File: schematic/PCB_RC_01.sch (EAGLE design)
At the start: 0 parts

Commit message: Completed PCB
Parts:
- added 12V, 5V, JET: GRN, led:LED5MM
- added 3V3: YEL, led:LED5MM
- added F1: 10A, fuse:FUSEBLANK_5X20MM
- added F2: 5A, fuse:FUSEBLANK_5X20MM
- added IC1: 3V3REG, pinhead:PINHD-1X4
- added IC2: 5VREG, SparkFun-IC-Power:V_REG_LD1117VXX
- added IC3-1, IC3-2: 12VREG, pinhead:PINHD-1X4
- added J1: 282836-2, 5mm Terminal Block:282836-2
- added J2: JETSON, 5mm Terminal Block:282836-2
- added J3: ARDUINO, 5mm Terminal Block:282836-2
- added J4: RESV, 5mm Terminal Block:282836-2
- added J6: USB1, SparkFun-Connectors:USB_B_PTH
- added J7: USB2, SparkFun-Connectors:USB_B_PTH
- added JP1: 5V PORT, pinhead:PINHD-2X5
- added JP2: 3V3 PORT, pinhead:PINHD-2X5
- added MOT, PWR: RED, led:LED5MM
- added R1, R2, R3, R4, R5, R6: 10K, rcl:R-US_V234/12
- added SW1: PWR, switch:2P2T
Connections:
- new net 12VREG: F2.1, IC3-1.3, IC3-1.4, J3.1, J4.1, R4.1
- new net 3V3REG: IC1.2, JP2.1, JP2.3, JP2.5, JP2.7, JP2.9, R3.1
- new net 5VREG: IC2.OUT, J6.VBUS, J7.VBUS, JP1.1, JP1.3, JP1.5, JP1.7, JP1.9, R2.1
- new net GND: 12V.C, 3V3.C, 5V.C, IC1.1, IC2.GND, IC3-1.1, IC3-1.2, IC3-2.1, IC3-2.2, J1.2, J2.2, J3.2, J4.2, J6.GND, J7.GND, JET.C, JP1.10, JP1.2, JP1.4, JP1.6, JP1.8, JP2.10, JP2.2, JP2.4, JP2.6, JP2.8, MOT.C, PWR.C, SW1.2.1, SW1.2.2
- new net JETSON: F2.2, J2.1, R5.1
- new net N$1: PWR.A, R1.2
- new net N$2: 5V.A, R2.2
- new net N$3: 3V3.A, R3.2
- new net N$4: 12V.A, R4.2
- new net N$5: MOT.A, R5.2
- new net N$6: JET.A, R6.2
- new net VBATT: J1.1, SW1.1.1, SW1.1.2
- new net VFUSE: F1.2, IC1.3, IC1.4, IC2.IN, IC3-2.3, IC3-2.4, R6.1
- new net VSWITCH: F1.1, R1.1, SW1.3.1, SW1.3.2

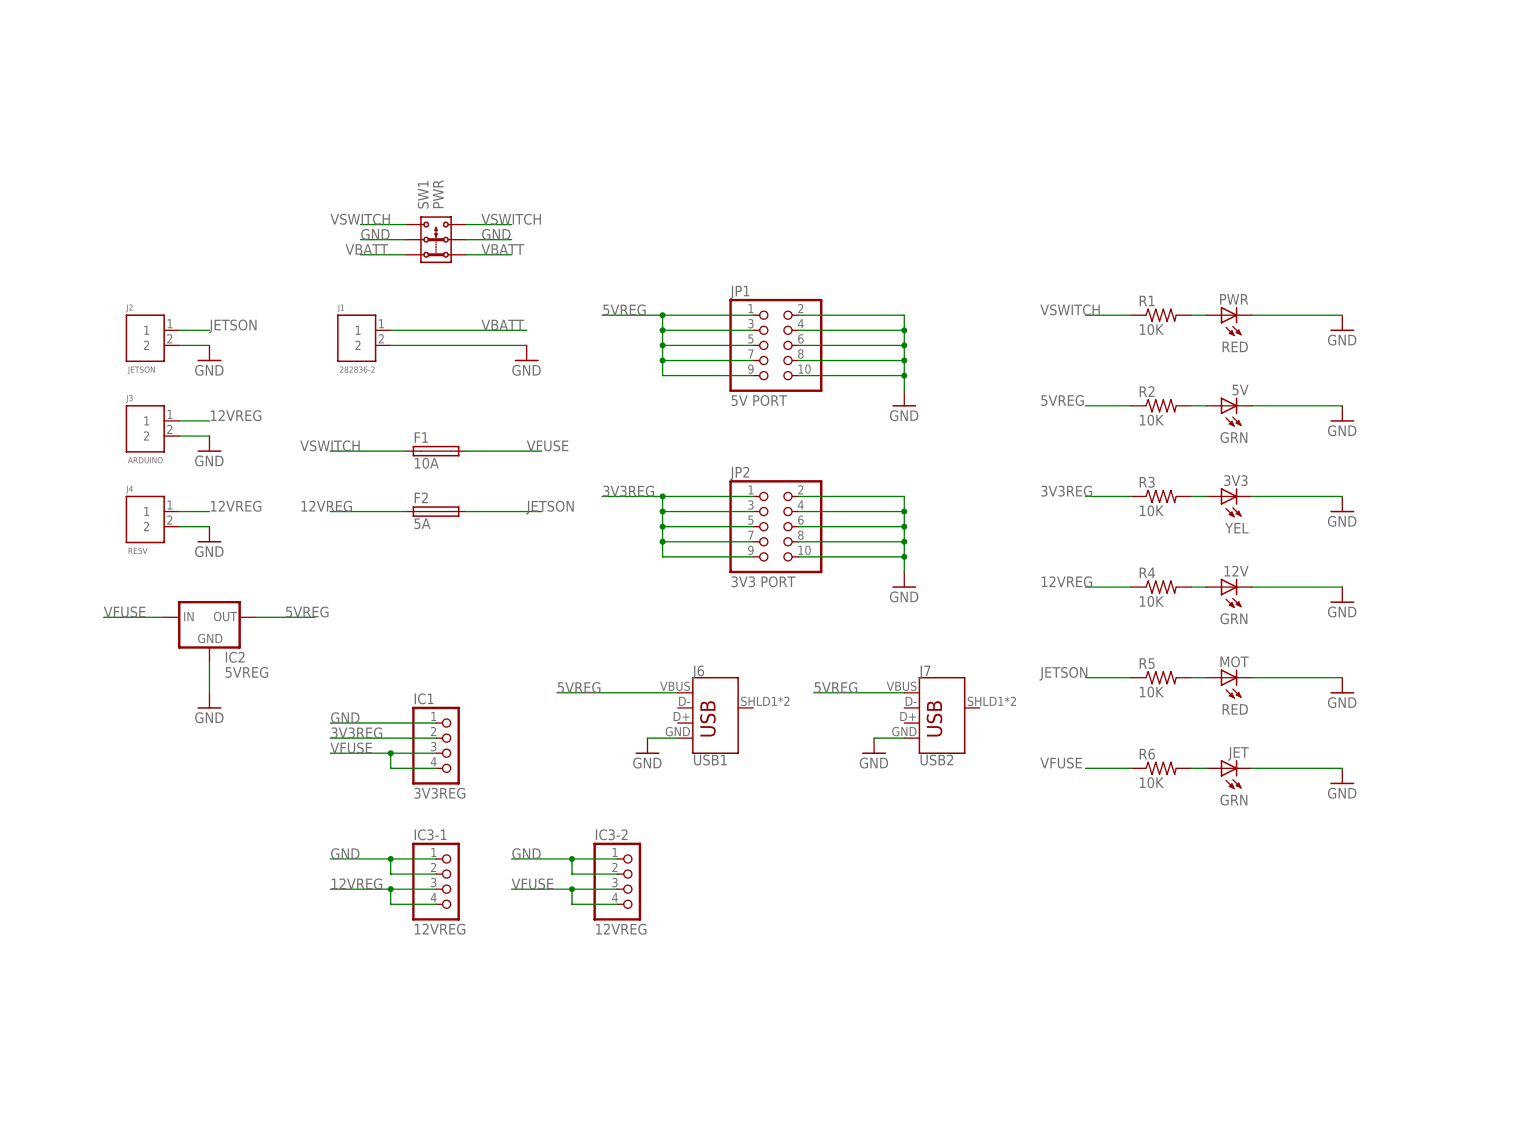
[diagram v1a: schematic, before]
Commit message: Completed schematic and docs
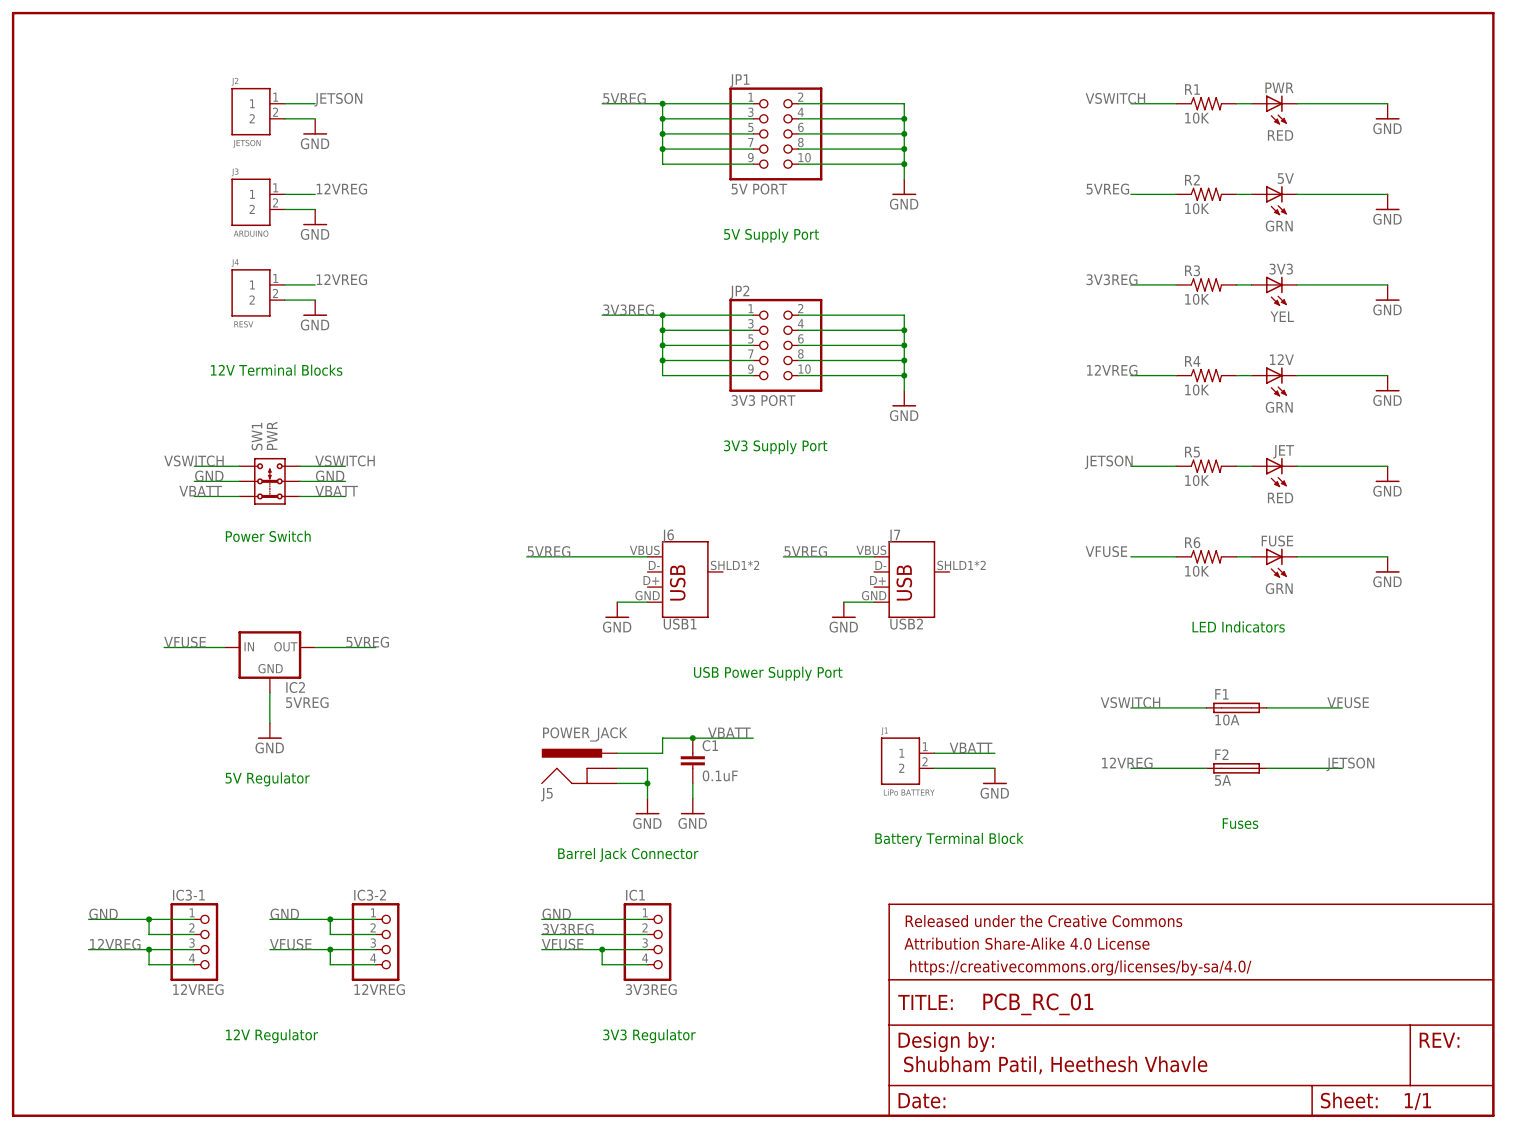
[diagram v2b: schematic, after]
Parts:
- removed MOT: RED, led:LED5MM
- added C1: 0.1uF, rcl:C-EU025-024X044
- added FRAME1: FRAME-LETTERNO_PACKAGE, SparkFun-Aesthetics:FRAME-LETTERNO_PACKAGE
- added FUSE: GRN, led:LED5MM
- added J5: POWER_JACK, SparkFun-Connectors:POWER_JACK
- J1: value 282836-2 -> LiPo BATTERY
- JET: value GRN -> RED
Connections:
- net GND: now also C1.2, FUSE.C, J5.GND, J5.GNDBREAK; no longer MOT.C
- net N$5: now also JET.A; no longer MOT.A
- net N$6: now also FUSE.A; no longer JET.A
- net VBATT: now also C1.1, J5.PWR
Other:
- note added: "12V Regulator"
- note added: "12V Terminal Blocks"
- note added: "3V3 Regulator"
- note added: "3V3 Supply Port"
- note added: "5V Regulator"
- note added: "5V Supply Port"
- note added: "Barrel Jack Connector"
- note added: "Battery Terminal Block"
- note added: "Fuses"
- note added: "LED Indicators"
- note added: "Power Switch"
- note added: "Shubham Patil, Heethesh Vhavle"
- note added: "USB Power Supply Port"
- moved on the sheet: 12V, 3V3, 5V, F1, F2, IC1, IC2, IC3-1, IC3-2, J1, J2, J3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

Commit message: Version 2 with layout complete
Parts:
- removed SW1: PWR, switch:2P2T
- 12V, 3V3, 5V, FUSE, JET, PWR: device led:LED5MM -> led:LED3MM
- C1: value 0.1uF -> 330uF; device rcl:C-EU025-024X044 -> rcl:C-US025-050X050
- IC2: device SparkFun-IC-Power:V_REG_LD1117VXX -> pinhead:PINHD-1X4
- J1: device 5mm Terminal Block:282836-2 -> XT60:XT60
- J2, J3, J4: device 5mm Terminal Block:282836-2 -> SparkFun-Connectors:POWER_JACK
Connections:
- removed net VSWITCH: F1.1, R1.1, SW1.3.1, SW1.3.2
- net 12VREG: now also J3.PWR, J4.PWR; no longer J3.1, J4.1
- net 3V3REG: now also IC1.1; no longer IC1.2
- net 5VREG: now also IC2.1; no longer IC2.OUT
- net GND: now also IC1.2, IC2.2, J1.GND, J2.GND, J2.GNDBREAK, J3.GND, J3.GNDBREAK, J4.GND, J4.GNDBREAK; no longer IC1.1, IC2.GND, J1.2, J2.2, J3.2, J4.2, SW1.2.1, SW1.2.2
- net JETSON: now also J2.PWR; no longer J2.1
- net VBATT: now also F1.1, J1.VCC, R1.1; no longer J1.1, SW1.1.1, SW1.1.2
- net VFUSE: now also IC2.3; no longer IC1.4, IC2.IN
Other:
- note added: "Heethesh Vhavle, Shubham Patil (Delta Autonomy)"
- note added: "RC Car Power Supply Board"
- note added: "v02"
- note removed: "Power Switch"
- note removed: "Shubham Patil, Heethesh Vhavle"
- moved on the sheet: C1, IC1, IC3-2, J2, J3, J4, J5
